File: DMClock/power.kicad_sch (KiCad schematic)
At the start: 0 parts

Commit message: adding mplabxide init files
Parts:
- added C1: 0.1uF, Capacitor_SMD:C_0805_2012Metric, symbol Device:C
- added J1: Barrel_Jack_Switch, Connector_BarrelJack:BarrelJack_Horizontal, symbol Connector:Barrel_Jack_Switch
- added J2: Conn_01x02 (9v battery), Connector_Molex:Molex_KK-254_AE-6410-02A_1x02_P2.54mm_Vertical, symbol Connector_Generic:Conn_01x02
- added SW5: SW_SPDT, Button_Switch_THT:SW_CuK_OS102011MA1QN1_SPDT_Angled, symbol Switch:SW_SPDT
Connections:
- new net: C1.1, J1.1, J1.3, J2.1 (Pin_1), SW5.2 (B)
- new net GND: C1.2, J1.2, J2.2 (Pin_2), SW5.3 (C)
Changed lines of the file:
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@@
 (kicad_sch (version 20230121) (generator eeschema)
   (paper "A4")
-  (hierarchical_label "Barrel Jack" (shape output) (at 69.596 106.807 0) (fields_autoplaced)
+  (junction (at 73.787 121.4101) (diameter 0) (color 0 0 0 0)
+  )
+  (junction (at 68.834 109.982) (diameter 0) (color 0 0 0 0)
+  )
+  (junction (at 71.882 109.982) (diameter 0) (color 0 0 0 0)
+  )
+  (junction (at 71.882 115.316) (diameter 0) (color 0 0 0 0)
+  )
+  (wire (pts (xy 65.532 121.412) (xy 73.787 121.412))
+    (stroke (width 0) (type default))
+  )
+  (wire (pts (xy 68.834 108.966) (xy 68.834 109.982))
+    (stroke (width 0) (type default))
+  )
+  (wire (pts (xy 68.834 116.332) (xy 68.834 109.982))
+    (stroke (width 0) (type default))
+  )
+  (wire (pts (xy 68.834 109.982) (xy 71.882 109.982))
+    (stroke (width 0) (type default))
+  )
+  (wire (pts (xy 73.787 117.856) (xy 73.787 121.4101))
+    (stroke (width 0) (type default))
+  )
+  (wire (pts (xy 73.787 121.4101) (xy 73.787 121.412))
+    (stroke (width 0) (type default))
+  )
+  (wire (pts (xy 68.8364 101.346) (xy 68.834 101.346))
+    (stroke (width 0) (type default))
+  )
+  (wire (pts (xy 65.532 118.872) (xy 71.882 118.872))
+    (stroke (width 0) (type default))
+  )
+  (wire (pts (xy 76.073 117.856) (xy 73.787 117.856))
+    (stroke (width 0) (type default))
+  )
+  (wire (pts (xy 71.882 115.316) (xy 76.073 115.316))
+    (stroke (width 0) (type default))
+  )
+  (wire (pts (xy 71.882 109.982) (xy 83.185 109.982))
+    (stroke (width 0) (type default))
+  )
+  (wire (pts (xy 68.8364 101.346) (xy 68.8364 99.4438))
+    (stroke (width 0) (type default))
+  )
+  (wire (pts (xy 71.882 118.872) (xy 71.882 115.316))
+    (stroke (width 0) (type default))
+  )
+  (wire (pts (xy 65.532 116.332) (xy 68.834 116.332))
+    (stroke (width 0) (type default))
+  )
+  (wire (pts (xy 71.882 109.982) (xy 71.882 115.316))
+    (stroke (width 0) (type default))
+  )
+  (hierarchical_label "HV" (shape output) (at 135.128 103.251 0) (fields_autoplaced)
     (effects (font (size 1.27 1.27)) (justify left))
   )
-  (hierarchical_label "HV" (shape output) (at 69.723 102.362 0) (fields_autoplaced)
-    (effects (font (size 1.27 1.27)) (justify left))
-  )
-  (hierarchical_label "9V" (shape input) (at 69.596 110.109 0) (fields_autoplaced)
-    (effects (font (size 1.27 1.27)) (justify left))
+  (symbol (lib_id "Switch:SW_SPDT") (at 88.265 109.982 0) (unit 1)
+    (in_bom yes) (on_board yes) (dnp no) (fields_autoplaced)
+    (property "Reference" "SW5" (at 88.265 101.6 0)
+      (effects (font (size 1.27 1.27)))
+    )
+    (property "Value" "SW_SPDT" (at 88.265 104.14 0)
+      (effects (font (size 1.27 1.27)))
+    )
+    (property "Footprint" "Button_Switch_THT:SW_CuK_OS102011MA1QN1_SPDT_Angled" (at 88.265 109.982 0)
+      (effects (font (size 1.27 1.27)) hide)
+    )
+    (property "Datasheet" "~" (at 88.265 117.602 0)
+      (effects (font (size 1.27 1.27)) hide)
+    )
+    (pin "2")
+    (pin "1")
+    (pin "3")
+    (instances
+      (project "DMClock"
+        (path "/b42b345f-a3f2-4eff-9109-2f4619119d33/e2b2635d-0e87-4f37-9170-e83d5f5e5877"
+          (reference "SW5") (unit 1)
+        )
+      )
+    )
+  )
+  (symbol (lib_id "Connector_Generic:Conn_01x02") (at 81.153 115.316 0) (unit 1)
+    (in_bom yes) (on_board yes) (dnp no) (fields_autoplaced)
+    (property "Reference" "J2" (at 82.423 120.142 90)
+      (effects (font (size 1.27 1.27)) (justify right))
+    )
+    (property "Value" "Conn_01x02 (9v battery)" (at 79.883 120.142 90)
+      (effects (font (size 1.27 1.27)) (justify right))
+    )
+    (property "Footprint" "Connector_Molex:Molex_KK-254_AE-6410-02A_1x02_P2.54mm_Vertical" (at 81.153 115.316 0)
+      (effects (font (size 1.27 1.27)) hide)
+    )
+    (property "Datasheet" "~" (at 81.153 115.316 0)
+      (effects (font (size 1.27 1.27)) hide)
+    )
+    (pin "2")
+    (pin "1")
+    (instances
+      (project "DMClock"
+        (path "/b42b345f-a3f2-4eff-9109-2f4619119d33/e2b2635d-0e87-4f37-9170-e83d5f5e5877"
+          (reference "J2") (unit 1)
+        )
+      )
+    )
+  )
+  (symbol (lib_id "Connector:Barrel_Jack_Switch") (at 57.912 118.872 0) (unit 1)
+    (in_bom yes) (on_board yes) (dnp no) (fields_autoplaced)
+    (property "Reference" "J1" (at 57.912 109.982 0)
+      (effects (font (size 1.27 1.27)))
+    )
+    (property "Value" "Barrel_Jack_Switch" (at 57.912 112.522 0)
+      (effects (font (size 1.27 1.27)))
+    )
+    (property "Footprint" "Connector_BarrelJack:BarrelJack_Horizontal" (at 59.182 119.888 0)
+      (effects (font (size 1.27 1.27)) hide)
+    )
+    (property "Datasheet" "~" (at 59.182 119.888 0)
+      (effects (font (size 1.27 1.27)) hide)
+    )
+    (pin "2")
+    (pin "1")
+    (pin "3")
+    (instances
+      (project "DMClock"
+        (path "/b42b345f-a3f2-4eff-9109-2f4619119d33/e2b2635d-0e87-4f37-9170-e83d5f5e5877"
+          (reference "J1") (unit 1)
+        )
+      )
+    )
+  )
+  (symbol (lib_id "power:GND") (at 93.345 112.522 90) (unit 1)
+    (in_bom yes) (on_board yes) (dnp no) (fields_autoplaced)
+    (property "Reference" "#PWR026" (at 99.695 112.522 0)
+      (effects (font (size 1.27 1.27)) hide)
+    )
+    (property "Value" "GND" (at 96.52 112.522 90)
+      (effects (font (size 1.27 1.27)) (justify right))
+    )
+    (property "Footprint" "" (at 93.345 112.522 0)
+      (effects (font (size 1.27 1.27)) hide)
+    )
+    (property "Datasheet" "" (at 93.345 112.522 0)
+      (effects (font (size 1.27 1.27)) hide)
+    )
+    (pin "1")
+    (instances
+      (project "DMClock"
+        (path "/b42b345f-a3f2-4eff-9109-2f4619119d33/e2b2635d-0e87-4f37-9170-e83d5f5e5877"
+          (reference "#PWR026") (unit 1)
+        )
+      )
+    )
+  )
+  (symbol (lib_id "power:GND") (at 73.787 121.4101 0) (unit 1)
+    (in_bom yes) (on_board yes) (dnp no) (fields_autoplaced)
+    (property "Reference" "#PWR027" (at 73.787 127.7601 0)
+      (effects (font (size 1.27 1.27)) hide)
+    )
+    (property "Value" "GND" (at 73.787 125.8551 0)
+      (effects (font (size 1.27 1.27)))
+    )
+    (property "Footprint" "" (at 73.787 121.4101 0)
+      (effects (font (size 1.27 1.27)) hide)
+    )
+    (property "Datasheet" "" (at 73.787 121.4101 0)
+      (effects (font (size 1.27 1.27)) hide)
+    )
+    (pin "1")
+    (instances
+      (project "DMClock"
+        (path "/b42b345f-a3f2-4eff-9109-2f4619119d33/e2b2635d-0e87-4f37-9170-e83d5f5e5877"
+          (reference "#PWR027") (unit 1)
+        )
+      )
+    )
+  )
+  (symbol (lib_id "power:GND") (at 68.8364 99.4438 180) (unit 1)
+    (in_bom yes) (on_board yes) (dnp no) (fields_autoplaced)
+    (property "Reference" "#PWR025" (at 68.8364 93.0938 0)
+      (effects (font (size 1.27 1.27)) hide)
+    )
+    (property "Value" "GND" (at 68.8364 94.3638 0)
+      (effects (font (size 1.27 1.27)))
+    )
+    (property "Footprint" "" (at 68.8364 99.4438 0)
+      (effects (font (size 1.27 1.27)) hide)
+    )
+    (property "Datasheet" "" (at 68.8364 99.4438 0)
+      (effects (font (size 1.27 1.27)) hide)
+    )
+    (pin "1")
+    (instances
+      (project "DMClock"
+        (path "/b42b345f-a3f2-4eff-9109-2f4619119d33/e2b2635d-0e87-4f37-9170-e83d5f5e5877"
+          (reference "#PWR025") (unit 1)
+        )
+      )
+    )
+  )
+  (symbol (lib_id "Device:C") (at 68.834 105.156 180) (unit 1)
+    (in_bom yes) (on_board yes) (dnp no) (fields_autoplaced)
+    (property "Reference" "C1" (at 72.771 103.886 0)
+      (effects (font (size 1.27 1.27)) (justify right))
+    )
+    (property "Value" "0.1uF" (at 72.771 106.426 0)
+      (effects (font (size 1.27 1.27)) (justify right))
+    )
+    (property "Footprint" "Capacitor_SMD:C_0805_2012Metric" (at 67.8688 101.346 0)
+      (effects (font (size 1.27 1.27)) hide)
+    )
+    (property "Datasheet" "~" (at 68.834 105.156 0)
+      (effects (font (size 1.27 1.27)) hide)
+    )
+    (pin "2")
+    (pin "1")
+    (instances
+      (project "DMClock"
+        (path "/b42b345f-a3f2-4eff-9109-2f4619119d33/e2b2635d-0e87-4f37-9170-e83d5f5e5877"
+          (reference "C1") (unit 1)
+        )
+      )
+    )
   )
 )

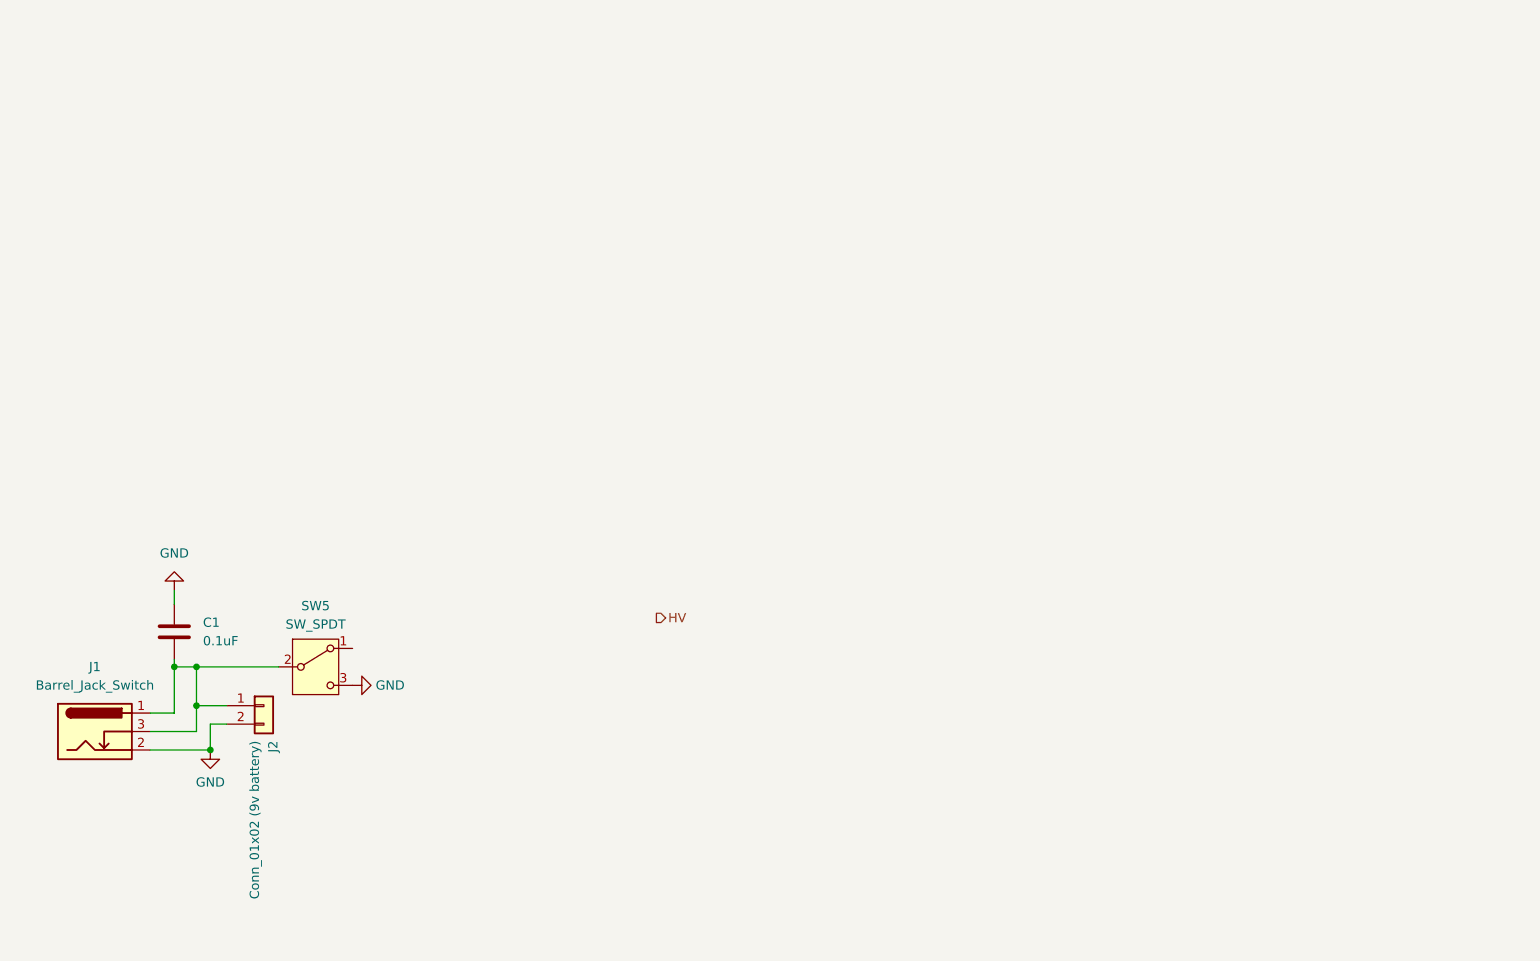
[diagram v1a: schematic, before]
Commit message: more modules added, still need to add a lot of footprints and see if there exist any sd card libraries for use with i2s
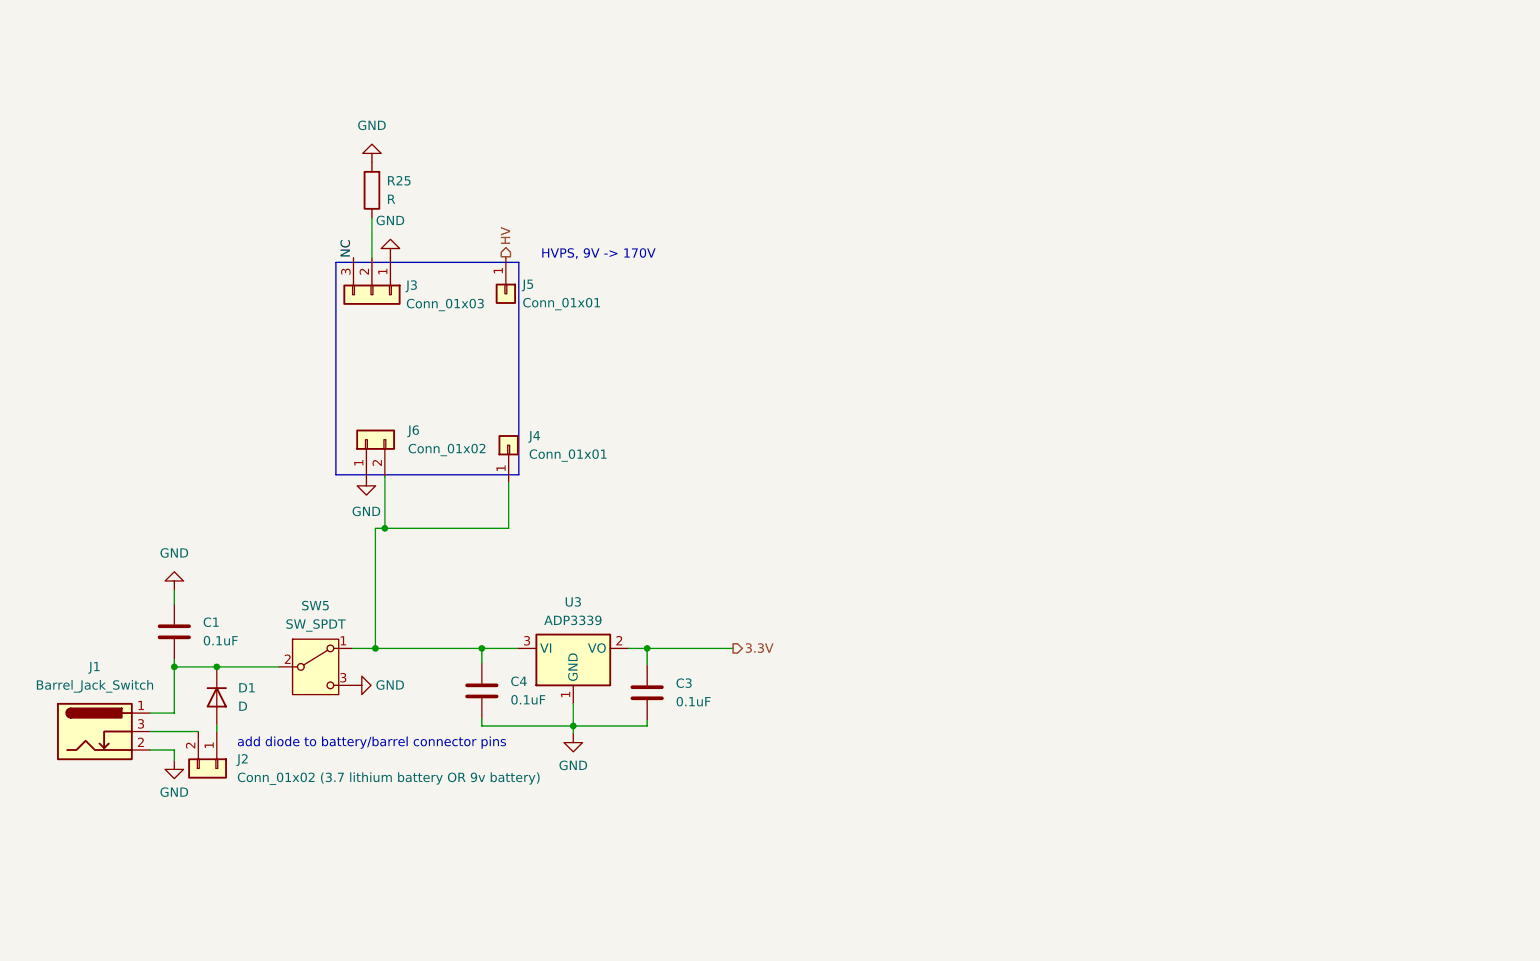
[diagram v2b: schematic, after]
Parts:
- added C3, C4: 0.1uF, Capacitor_SMD:C_0805_2012Metric, symbol Device:C
- added D1: D, symbol Device:D
- added J3: Conn_01x03, symbol Connector_Generic:Conn_01x03
- added J4, J5: Conn_01x01, symbol Connector_Generic:Conn_01x01
- added J6: Conn_01x02, symbol Connector_Generic:Conn_01x02
- added R25: R, Resistor_THT:R_Axial_DIN0204_L3.6mm_D1.6mm_P2.54mm_Vertical, symbol Device:R
- added U3: ADP3339, Package_TO_SOT_SMD:SOT-223-3_TabPin2, symbol Regulator_Linear:AMS1117-3.3
- J2: value Conn_01x02 (9v battery) -> Conn_01x02 (3.7 lithium battery OR 9v battery)
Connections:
- net GND: now also C3.1, C4.1, J3.1 (Pin_1), J6.1 (Pin_1), R25.2, U3.1 (GND); no longer J2.2 (Pin_2)
- net HV: now also J5.1 (Pin_1)
- net at SW5.1 (A): now also C4.2, J4.1 (Pin_1), J6.2 (Pin_2), U3.3 (VI)
- net at C1.1, J1.1, SW5.2 (B): now also D1.1 (K); no longer J1.3, J2.1 (Pin_1)
- new net: J1.3, J2.2 (Pin_2)
- new net: D1.2 (A), J2.1 (Pin_1)
- new net: J3.2 (Pin_2), R25.1
- new net 3.3V: C3.2, U3.2 (VO)
- new net NC: J3.3 (Pin_3)
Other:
- note added: "HVPS, 9V -> 170V"
- note added: "add diode to battery/barrel connector pins"

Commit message: need to work on hvps logic converter
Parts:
- removed U3: ADP3339, Package_TO_SOT_SMD:SOT-223-3_TabPin2, symbol Regulator_Linear:AMS1117-3.3
- added C2: 10uF, Capacitor_SMD:C_0805_2012Metric, symbol Device:C
- added C5: 0.1uF, Capacitor_SMD:C_0805_2012Metric, symbol Device:C
- added C6, C8: 22uF, Capacitor_SMD:C_0805_2012Metric, symbol Device:C
- added C7: 22nF, Capacitor_SMD:C_0805_2012Metric, symbol Device:C
- added C9: 470pF, Capacitor_SMD:C_0805_2012Metric, symbol Device:C
- added IC1: MP2338GTL-Z, Footprints:MP2338GTLZ, symbol MP2338GTL-Z:MP2338GTL-Z
- added L1: 6.8uH, symbol Device:L
- added R4: 191k, Resistor_THT:R_Axial_DIN0204_L3.6mm_D1.6mm_P2.54mm_Vertical, symbol Device:R
- added R5: 49.9k, Resistor_THT:R_Axial_DIN0204_L3.6mm_D1.6mm_P2.54mm_Vertical, symbol Device:R
- added R6: 100k, Resistor_THT:R_Axial_DIN0204_L3.6mm_D1.6mm_P2.54mm_Vertical, symbol Device:R
- added R7: 10k, Resistor_THT:R_Axial_DIN0204_L3.6mm_D1.6mm_P2.54mm_Vertical, symbol Device:R
- added R8: 9.09k, Resistor_THT:R_Axial_DIN0204_L3.6mm_D1.6mm_P2.54mm_Vertical, symbol Device:R
- added R9: 51k, Resistor_THT:R_Axial_DIN0204_L3.6mm_D1.6mm_P2.54mm_Vertical, symbol Device:R
- C3: value 0.1uF -> 10uF
- J2: value Conn_01x02 (3.7 lithium battery OR 9v battery) -> (12v LiPo battery)
- renumbered J6 to J3, J3 to J4, J4 to J6, R25 to R3, SW5 to SW2
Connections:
- net 3.3V: now also C6.1, C8.2, C9.1, L1.1; no longer C3.2
- net GND: now also C3.2, C2.2, C6.2, C7.1, C8.1, IC1.4 (GND), R5.2, R8.2; no longer C3.1
- net 12V: now reaches C4.2, J3.2 (Pin_2), J6.1 (Pin_1), SW2.1 (A)
- net 12V: now also C3.1, C2.1, IC1.2 (VIN), R4.1
- new net: IC1.1 (PG), R6.2
- new net: C5.1, IC1.3 (SW), L1.2
- new net: C5.2, IC1.5 (BST)
- new net: IC1.6 (EN), R4.2, R5.1
- new net: C7.2, IC1.7 (SS)
- new net: IC1.8 (FB), R7.1
- new net: C9.2, R7.2, R8.1, R9.2
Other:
- note added: "double check this"
- moved on the sheet: J3

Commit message: just need to finish pcb
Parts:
- removed J5, J6: Conn_01x01, symbol Connector_Generic:Conn_01x01
- removed R3: R, Resistor_THT:R_Axial_DIN0204_L3.6mm_D1.6mm_P2.54mm_Vertical, symbol Device:R
- D1: footprint (none) -> Diode_THT:D_A-405_P2.54mm_Vertical_AnodeUp
- J3: footprint (none) -> Connector_PinHeader_2.54mm:PinHeader_1x02_P2.54mm_Vertical
- J4: footprint (none) -> Connector_PinHeader_2.54mm:PinHeader_1x03_P2.54mm_Vertical
- L1: footprint (none) -> Inductor_SMD:L_0805_2012Metric
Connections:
- net 12V: now also J4.1 (Pin_1); no longer J3.2 (Pin_2)
- net GND: now also J4.2 (Pin_2); no longer J4.1 (Pin_1), SW2.3 (C)
- net HV: now also J3.2 (Pin_2)
- net NC: no longer names the net of J4.3 (Pin_3)
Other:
- moved on the sheet: J3, J4
